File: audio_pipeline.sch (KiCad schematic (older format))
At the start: 15 parts

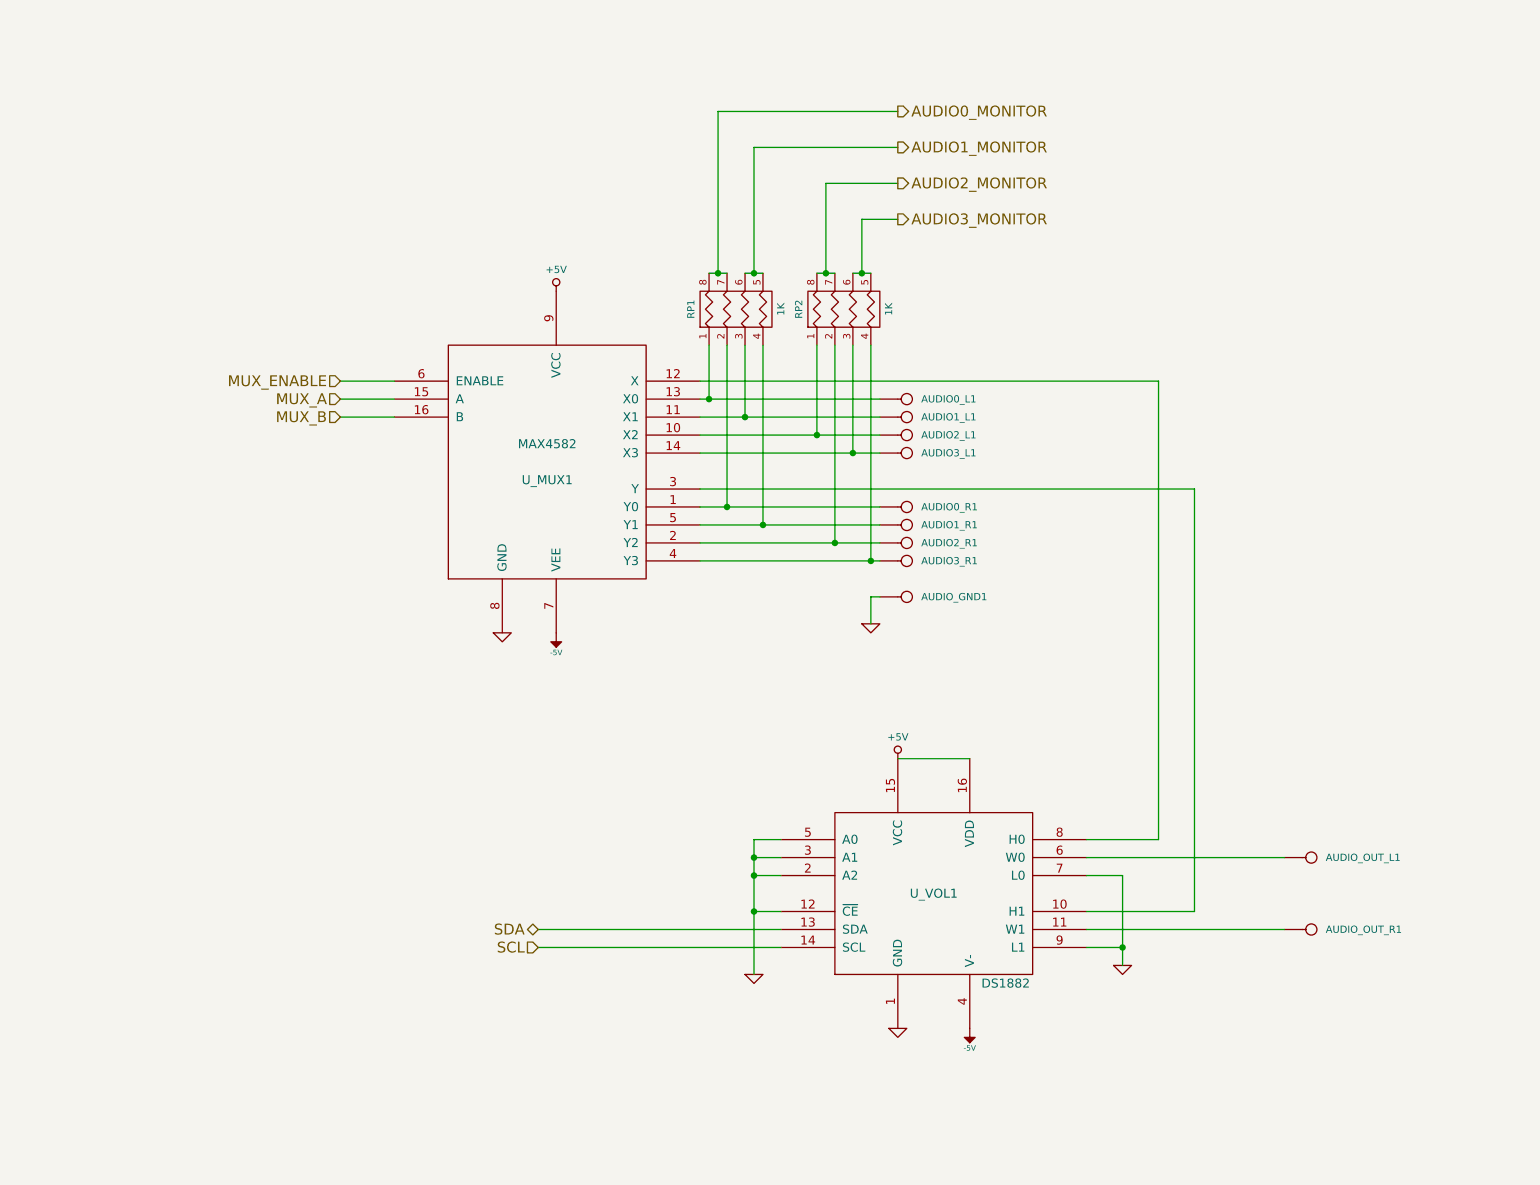
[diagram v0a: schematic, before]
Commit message: Switching to atmega164, muxing the two seven-segs instead of using IO exapander.
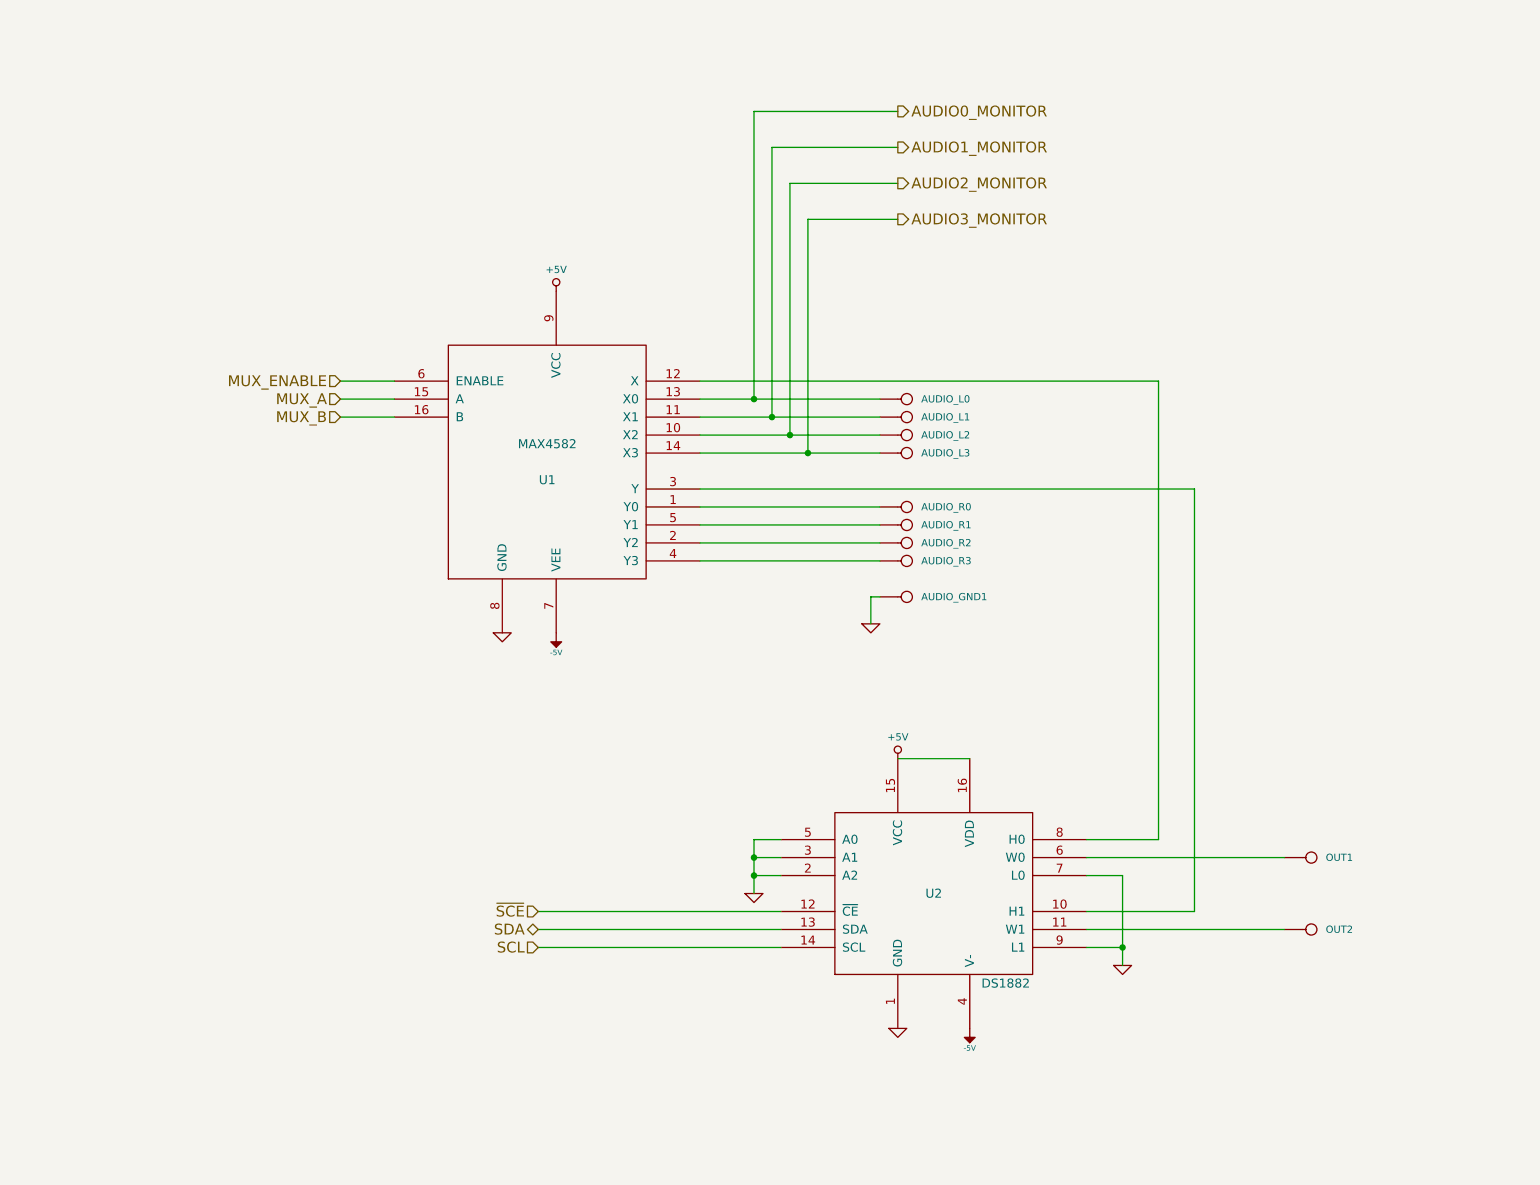
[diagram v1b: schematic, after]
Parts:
- removed RP1, RP2: 1K, symbol R_PACK4
- renumbered AUDIO0_L1 to AUDIO_L0, AUDIO1_L1 to AUDIO_L1, AUDIO2_L1 to AUDIO_L2, AUDIO3_L1 to AUDIO_L3, AUDIO0_R1 to AUDIO_R0, AUDIO1_R1 to AUDIO_R1, AUDIO2_R1 to AUDIO_R2, AUDIO3_R1 to AUDIO_R3, AUDIO_OUT_L1 to OUT1, AUDIO_OUT_R1 to OUT2, U_MUX1 to U1, U_VOL1 to U2
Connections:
- net AUDIO0_MONITOR: now also AUDIO_L0.1, U1.13 (X0)
- net AUDIO1_MONITOR: now also AUDIO_L1.1, U1.11 (X1)
- net AUDIO2_MONITOR: now also AUDIO_L2.1, U1.10 (X2)
- net AUDIO3_MONITOR: now also AUDIO_L3.1, U1.14 (X3)
- net GND: no longer U2.12 (~CE)
- new net ~SCE: U2.12 (~CE)
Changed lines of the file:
@@
-EESchema Schematic File Version 2  date Sunday, May 06, 2012 01:54:04 pm
+EESchema Schematic File Version 2  date Saturday, June 02, 2012 10:08:47 pm
 LIBS:atmel
 LIBS:device
@@
 LIBS:BP5037
 LIBS:MCP23017
+LIBS:hdsp
+LIBS:lumex
 LIBS:kenwood-cache
 EELAYER 25  0
@@
 $Descr A4 11700 8267
 encoding utf-8
-Sheet 2 4
+Sheet 3 3
 Title ""
-Date "6 may 2012"
+Date "3 jun 2012"
 Rev ""
 Comp ""
@@
 Comment4 ""
 $EndDescr
-Connection ~ 5700 2200
-Wire Wire Line
-	5900 1900 5700 1900
-Wire Wire Line
-	5700 1900 5700 2200
-Connection ~ 5100 2200
-Wire Wire Line
-	5900 1500 5100 1500
-Wire Wire Line
-	5100 1500 5100 2200
-Wire Wire Line
-	5900 1300 4900 1300
+Wire Wire Line
+	5250 5750 3900 5750
+Wire Wire Line
+	5900 1700 5300 1700
+Wire Wire Line
+	5300 1700 5300 3100
+Wire Wire Line
+	5100 2900 5100 1300
+Connection ~ 5400 3200
+Connection ~ 5200 3000
 Wire Wire Line
 	4800 2800 7350 2800
@@
 	3900 5950 5250 5950
 Wire Wire Line
-	5450 2200 5550 2200
-Wire Wire Line
-	4850 2200 4950 2200
-Connection ~ 5650 3200
-Wire Wire Line
-	5650 2600 5650 3200
-Connection ~ 5450 3100
-Wire Wire Line
-	5450 2600 5450 3100
-Connection ~ 5050 3000
-Wire Wire Line
-	5050 2600 5050 3000
-Connection ~ 4850 2900
-Wire Wire Line
-	4850 2600 4850 2900
-Wire Wire Line
 	5800 3700 4800 3700
 Wire Wire Line
 	4800 3500 5800 3500
 Wire Wire Line
-	5800 3100 4800 3100
-Wire Wire Line
-	5800 2900 4800 2900
+	5800 3100 5300 3100
+Wire Wire Line
+	5300 3100 4800 3100
+Wire Wire Line
+	5800 2900 5100 2900
+Wire Wire Line
+	5100 2900 4800 2900
 Connection ~ 5100 5550
 Wire Wire Line
 	5100 5550 5250 5550
 Wire Wire Line
-	5100 6100 5100 5350
+	5100 5650 5100 5550
+Wire Wire Line
+	5100 5550 5100 5450
+Wire Wire Line
+	5100 5450 5100 5350
 Wire Wire Line
 	5100 5350 5250 5350
@@
 Connection ~ 7150 5950
 Wire Wire Line
-	7150 6050 7150 5550
+	7150 6050 7150 5950
+Wire Wire Line
+	7150 5950 7150 5550
 Wire Wire Line
 	7150 5550 6950 5550
@@
 Connection ~ 5100 5450
 Wire Wire Line
-	5100 5750 5250 5750
-Connection ~ 5100 5750
-Wire Wire Line
-	5800 3000 4800 3000
-Wire Wire Line
-	5800 3200 4800 3200
+	5800 3000 5200 3000
+Wire Wire Line
+	5200 3000 4800 3000
+Wire Wire Line
+	5800 3200 5400 3200
+Wire Wire Line
+	5400 3200 4800 3200
 Wire Wire Line
 	5800 3600 4800 3600
@@
 	5800 3800 4800 3800
 Wire Wire Line
-	4950 2600 4950 3500
-Connection ~ 4950 3500
-Wire Wire Line
-	5150 2600 5150 3600
-Connection ~ 5150 3600
-Wire Wire Line
-	5550 2600 5550 3700
-Connection ~ 5550 3700
-Wire Wire Line
-	5750 2600 5750 3800
-Connection ~ 5750 3800
-Wire Wire Line
-	5050 2200 5150 2200
-Wire Wire Line
-	5650 2200 5750 2200
-Wire Wire Line
 	3900 5850 5250 5850
 Wire Wire Line
@@
 Wire Wire Line
 	7550 3400 7550 5750
-Connection ~ 4900 2200
-Wire Wire Line
-	4900 1300 4900 2200
-Wire Wire Line
-	5500 2200 5500 1700
-Wire Wire Line
-	5500 1700 5900 1700
-Connection ~ 5500 2200
+Connection ~ 5100 2900
+Connection ~ 5300 3100
+Wire Wire Line
+	5100 1300 5900 1300
+Wire Wire Line
+	5200 3000 5200 1500
+Wire Wire Line
+	5200 1500 5900 1500
+Wire Wire Line
+	5400 3200 5400 1900
+Wire Wire Line
+	5400 1900 5900 1900
+Text HLabel 3900 5750 0    60   Input ~ 0
+~SCE
 Text HLabel 5900 1300 2    60   Output ~ 0
 AUDIO0_MONITOR
@@
 AUDIO3_MONITOR
 $Comp
-L GND #PWR035
+L GND #PWR5
 U 1 1 4F8F6783
 P 5750 4150
-F 0 "#PWR035" H 5750 4150 30  0001 C CNN
+F 0 "#PWR5" H 5750 4150 30  0001 C CNN
 F 1 "GND" H 5750 4080 30  0001 C CNN
 	1    5750 4150
@@
 SDA
 $Comp
-L R_PACK4 RP2
-U 1 1 4F8E114E
-P 5800 2400
-F 0 "RP2" H 5800 2850 40  0000 C CNN
-F 1 "1K" H 5800 2350 40  0000 C CNN
-	1    5800 2400
-	0    -1   -1   0
-$EndComp
-$Comp
-L MAX4582 U_MUX1
+L MAX4582 U1
 U 1 1 4F88F500
 P 3950 3250
-F 0 "U_MUX1" H 3950 3150 50  0000 C CNN
+F 0 "U1" H 3950 3150 50  0000 C CNN
 F 1 "MAX4582" H 3950 3350 50  0000 C CNN
 F 2 "MODULE" H 3950 3250 50  0001 C CNN
@@
 $EndComp
 $Comp
-L R_PACK4 RP1
-U 1 1 4F8E0FA7
-P 5200 2400
-F 0 "RP1" H 5200 2850 40  0000 C CNN
-F 1 "1K" H 5200 2350 40  0000 C CNN
-	1    5200 2400
-	0    -1   -1   0
-$EndComp
-$Comp
-L CONN_1 AUDIO3_R1
+L CONN_1 AUDIO_R3
 U 1 1 4F8E0F47
 P 5950 3800
-F 0 "AUDIO3_R1" H 6030 3800 40  0000 L CNN
+F 0 "AUDIO_R3" H 6030 3800 40  0000 L CNN
 F 1 "CONN_1" H 5950 3855 30  0001 C CNN
 	1    5950 3800
@@
 $EndComp
 $Comp
-L CONN_1 AUDIO2_R1
+L CONN_1 AUDIO_R2
 U 1 1 4F8E0F45
 P 5950 3700
-F 0 "AUDIO2_R1" H 6030 3700 40  0000 L CNN
+F 0 "AUDIO_R2" H 6030 3700 40  0000 L CNN
 F 1 "CONN_1" H 5950 3755 30  0001 C CNN
 	1    5950 3700
@@
 $EndComp
 $Comp
-L CONN_1 AUDIO1_R1
+L CONN_1 AUDIO_R1
 U 1 1 4F8E0F43
 P 5950 3600
-F 0 "AUDIO1_R1" H 6030 3600 40  0000 L CNN
+F 0 "AUDIO_R1" H 6030 3600 40  0000 L CNN
 F 1 "CONN_1" H 5950 3655 30  0001 C CNN
 	1    5950 3600
@@
 $EndComp
 $Comp
-L CONN_1 AUDIO0_R1
+L CONN_1 AUDIO_R0
 U 1 1 4F8E0F34
 P 5950 3500
-F 0 "AUDIO0_R1" H 6030 3500 40  0000 L CNN
+F 0 "AUDIO_R0" H 6030 3500 40  0000 L CNN
 F 1 "CONN_1" H 5950 3555 30  0001 C CNN
 	1    5950 3500
@@
 $EndComp
 $Comp
-L CONN_1 AUDIO3_L1
+L CONN_1 AUDIO_L3
 U 1 1 4F8E0EE4
 P 5950 3200
-F 0 "AUDIO3_L1" H 6030 3200 40  0000 L CNN
+F 0 "AUDIO_L3" H 6030 3200 40  0000 L CNN
 F 1 "CONN_1" H 5950 3255 30  0001 C CNN
 	1    5950 3200
@@
 $EndComp
 $Comp
-L CONN_1 AUDIO2_L1
+L CONN_1 AUDIO_L2
 U 1 1 4F8E0EBE
 P 5950 3100
-F 0 "AUDIO2_L1" H 6030 3100 40  0000 L CNN
+F 0 "AUDIO_L2" H 6030 3100 40  0000 L CNN
 F 1 "CONN_1" H 5950 3155 30  0001 C CNN
 	1    5950 3100
@@
 $EndComp
 $Comp
-L CONN_1 AUDIO1_L1
+L CONN_1 AUDIO_L1
 U 1 1 4F8E0EB9
 P 5950 3000
-F 0 "AUDIO1_L1" H 6030 3000 40  0000 L CNN
+F 0 "AUDIO_L1" H 6030 3000 40  0000 L CNN
 F 1 "CONN_1" H 5950 3055 30  0001 C CNN
 	1    5950 3000
@@
 $EndComp
 $Comp
-L CONN_1 AUDIO0_L1
+L CONN_1 AUDIO_L0
 U 1 1 4F8E0E20
 P 5950 2900
-F 0 "AUDIO0_L1" H 6030 2900 40  0000 L CNN
+F 0 "AUDIO_L0" H 6030 2900 40  0000 L CNN
 F 1 "CONN_1" H 5950 2955 30  0001 C CNN
 	1    5950 2900
@@
 $EndComp
 $Comp
-L -5V #PWR036
+L -5V #PWR8
 U 1 1 4F8E0C7B
 P 6300 6400
-F 0 "#PWR036" H 6300 6540 20  0001 C CNN
+F 0 "#PWR8" H 6300 6540 20  0001 C CNN
 F 1 "-5V" H 6300 6510 30  0000 C CNN
 	1    6300 6400
@@
 $EndComp
 $Comp
-L +5V #PWR037
+L +5V #PWR6
 U 1 1 4F8E0C5D
 P 5900 4900
-F 0 "#PWR037" H 5900 5050 40  0001 C CNN
+F 0 "#PWR6" H 5900 5050 40  0001 C CNN
 F 1 "+5V" H 5900 5020 40  0000 C CNN
 	1    5900 4900
@@
 $EndComp
 $Comp
-L GND #PWR038
+L GND #PWR7
 U 1 1 4F8E0C4F
 P 5900 6400
-F 0 "#PWR038" H 5900 6400 30  0001 C CNN
+F 0 "#PWR7" H 5900 6400 30  0001 C CNN
 F 1 "GND" H 5900 6330 30  0001 C CNN
 	1    5900 6400
@@
 $EndComp
 $Comp
-L GND #PWR039
+L GND #PWR4
 U 1 1 4F8E0C00
-P 5100 6100
-F 0 "#PWR039" H 5100 6100 30  0001 C CNN
-F 1 "GND" H 5100 6030 30  0001 C CNN
-	1    5100 6100
-	1    0    0    -1
-$EndComp
-$Comp
-L DS1882 U_VOL1
+P 5100 5650
+F 0 "#PWR4" H 5100 5650 30  0001 C CNN
+F 1 "GND" H 5100 5580 30  0001 C CNN
+	1    5100 5650
+	1    0    0    -1
+$EndComp
+$Comp
+L DS1882 U2
 U 1 1 4F8E0BE3
 P 6100 5650
-F 0 "U_VOL1" H 6100 5650 50  0000 C CNN
+F 0 "U2" H 6100 5650 50  0000 C CNN
 F 1 "DS1882" H 6500 5150 50  0000 C CNN
 F 2 "SOIC16" H 5700 5150 50  0001 C CNN
@@
 $EndComp
 $Comp
-L CONN_1 AUDIO_OUT_R1
+L CONN_1 OUT2
 U 1 1 4F8E0B2F
 P 8200 5850
-F 0 "AUDIO_OUT_R1" H 8280 5850 40  0000 L CNN
+F 0 "OUT2" H 8280 5850 40  0000 L CNN
 F 1 "CONN_1" H 8200 5905 30  0001 C CNN
 	1    8200 5850
@@
 $EndComp
 $Comp
-L CONN_1 AUDIO_OUT_L1
+L CONN_1 OUT1
 U 1 1 4F8E0B18
 P 8200 5450
-F 0 "AUDIO_OUT_L1" H 8280 5450 40  0000 L CNN
+F 0 "OUT1" H 8280 5450 40  0000 L CNN
 F 1 "CONN_1" H 8200 5505 30  0001 C CNN
 	1    8200 5450
@@
 $EndComp
 $Comp
-L GND #PWR040
+L GND #PWR9
 U 1 1 4F896654
 P 7150 6050
-F 0 "#PWR040" H 7150 6050 30  0001 C CNN
+F 0 "#PWR9" H 7150 6050 30  0001 C CNN
 F 1 "GND" H 7150 5980 30  0001 C CNN
 	1    7150 6050
@@
 $EndComp
 $Comp
-L +5V #PWR041
+L +5V #PWR2
 U 1 1 4F88F637
 P 4000 2300
-F 0 "#PWR041" H 4000 2450 40  0001 C CNN
+F 0 "#PWR2" H 4000 2450 40  0001 C CNN
 F 1 "+5V" H 4000 2420 40  0000 C CNN
 	1    4000 2300
@@
 $EndComp
 $Comp
-L -5V #PWR042
+L -5V #PWR3
 U 1 1 4F88F61F
 P 4000 4200
-F 0 "#PWR042" H 4000 4340 20  0001 C CNN
+F 0 "#PWR3" H 4000 4340 20  0001 C CNN
 F 1 "-5V" H 4000 4310 30  0000 C CNN
 	1    4000 4200
@@
 $EndComp
 $Comp
-L GND #PWR043
+L GND #PWR1
 U 1 1 4F88F5F7
 P 3700 4200
-F 0 "#PWR043" H 3700 4200 30  0001 C CNN
+F 0 "#PWR1" H 3700 4200 30  0001 C CNN
 F 1 "GND" H 3700 4130 30  0001 C CNN
 	1    3700 4200
